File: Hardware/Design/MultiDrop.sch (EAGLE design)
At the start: 13 parts

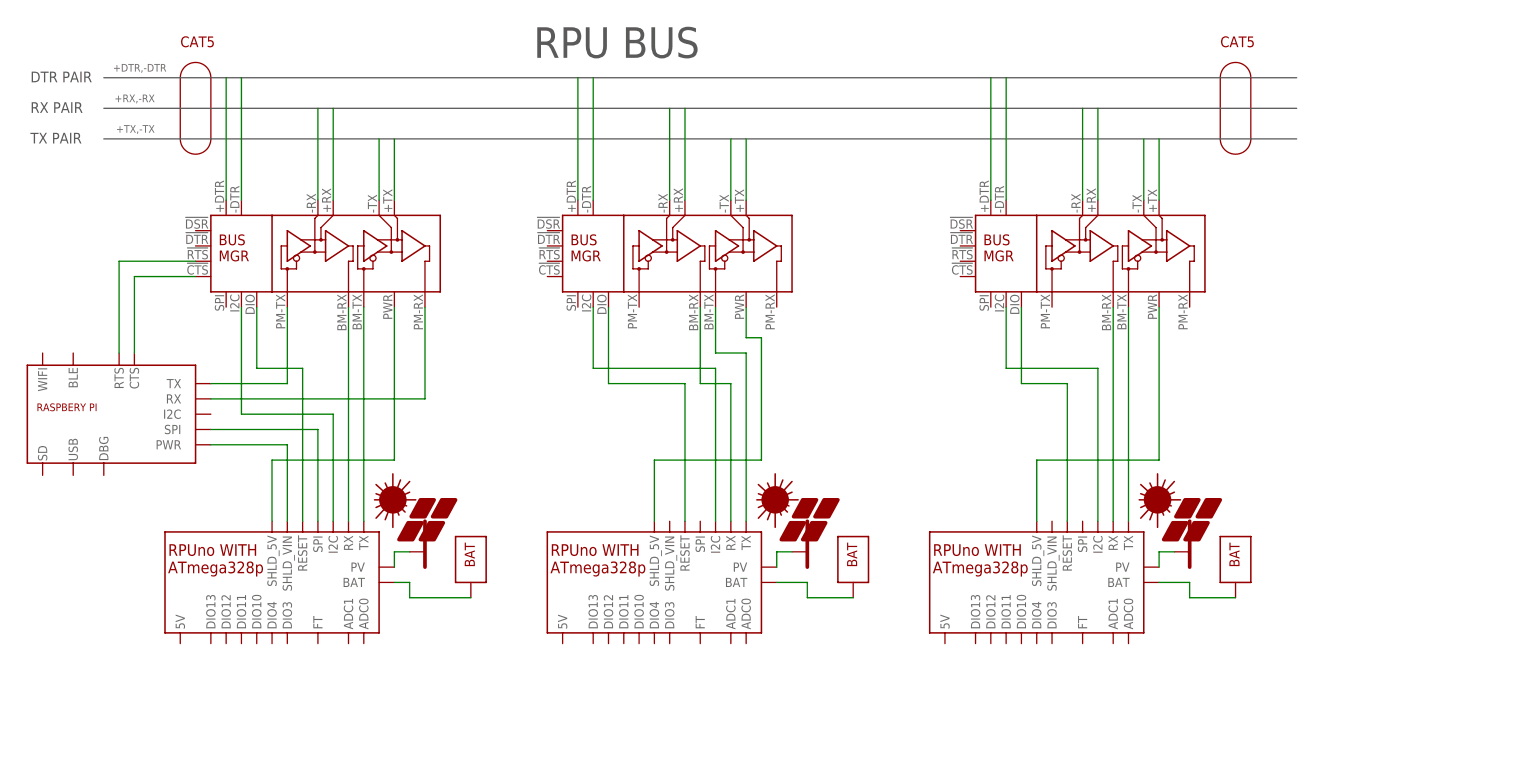
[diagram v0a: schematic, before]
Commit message: example is a little more refined
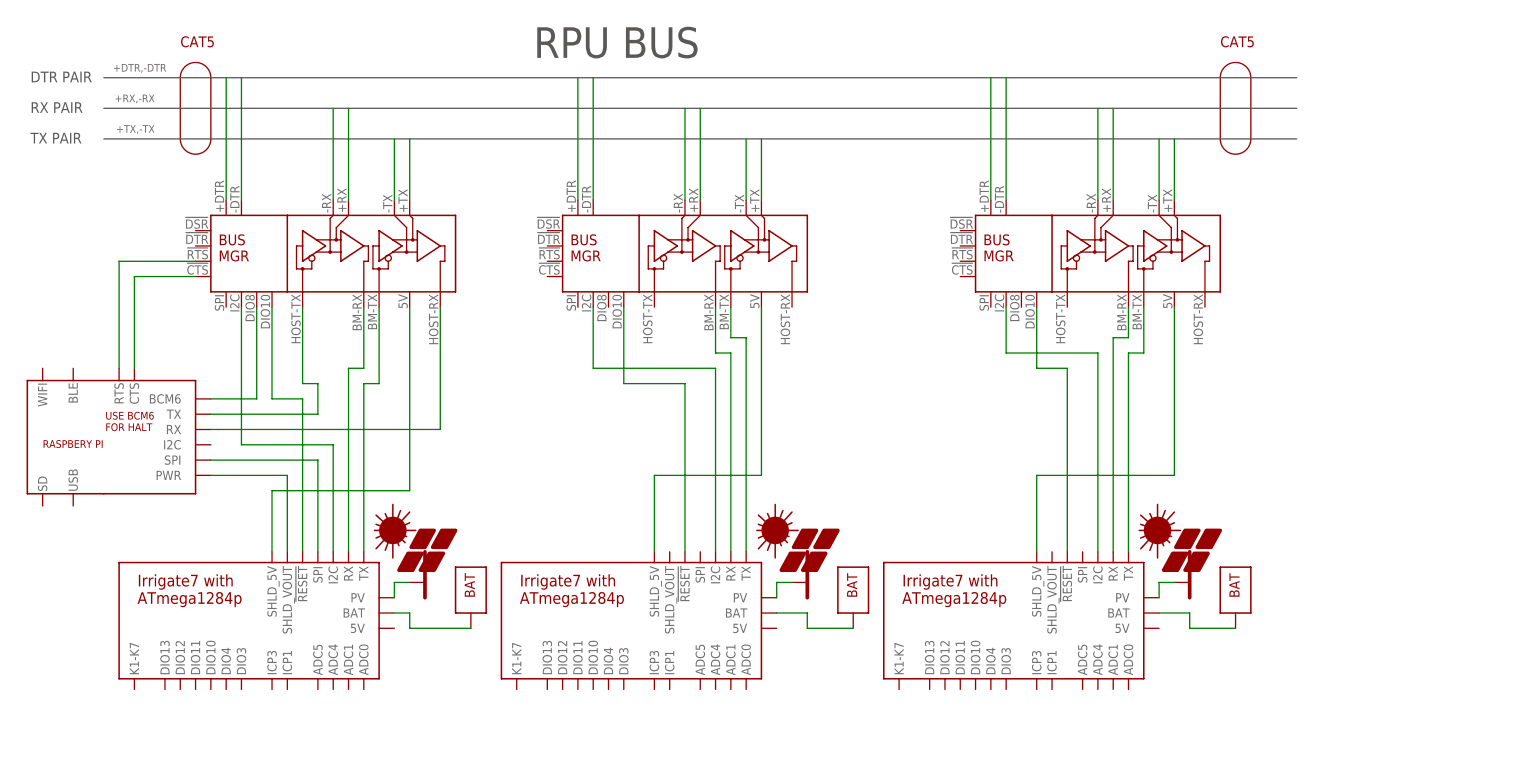
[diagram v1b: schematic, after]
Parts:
- removed BM1, BM2, BM3: (no value), Documentation:RPUNO
- added U$10: BUS_MGR, Documentation:BUS_MGR
- added U$6, U$8: IRRIGATE7, Documentation:IRRIGATE7
- U$2: value BUS_MGR -> IRRIGATE7; device Documentation:BUS_MGR -> Documentation:IRRIGATE7
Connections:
- new net N$13: U$10.DIO8, U$3.BCM6
- net +DTR: now also U$10.+DTR; no longer U$1.+DTR
- net +DTR1: now also U$5.+DTR; no longer U$2.+DTR
- net +DTR3: now also U$1.+DTR; no longer U$5.+DTR
- net +RX: now also U$10.+RX; no longer U$1.+RX
- net +RX1: now also U$5.+RX; no longer U$2.+RX
- net +RX3: now also U$1.+RX; no longer U$5.+RX
- net +TX: now also U$10.+TX; no longer U$1.+TX
- net +TX1: now also U$5.+TX; no longer U$2.+TX
- net +TX3: now also U$1.+TX; no longer U$5.+TX
- net -DTR: now also U$10.-DTR; no longer U$1.-DTR
- net -DTR1: now also U$5.-DTR; no longer U$2.-DTR
- net -DTR3: now also U$1.-DTR; no longer U$5.-DTR
- net -RX: now also U$10.-RX; no longer U$1.-RX
- net -RX1: now also U$5.-RX; no longer U$2.-RX
- net -RX3: now also U$1.-RX; no longer U$5.-RX
- net -TX: now also U$10.-TX; no longer U$1.-TX
- net -TX1: now also U$5.-TX; no longer U$2.-TX
- net -TX3: now also U$1.-TX; no longer U$5.-TX
- net N$1: now also U$10.BM_TX, U$8.TX; no longer BM2.TX, U$1.BM_TX
- net N$10: now also U$5.BM_TX, U$6.TX; no longer BM1.TX, U$2.BM_TX
- net N$11: now also U$5.BM_RX, U$6.RX; no longer BM1.RX, U$2.BM_RX
- net N$12: now also U$8.BAT; no longer BM2.BAT
- net N$14: now also U$1.BM_TX, U$2.TX; no longer BM3.TX, U$5.BM_TX
- net N$17: now also U$6.BAT; no longer BM1.BAT
- net N$2: now also U$10.BM_RX, U$8.RX; no longer BM2.RX, U$1.BM_RX
- net N$21: now also U$1.BM_RX, U$2.RX; no longer BM3.RX, U$5.BM_RX
- net N$29: now also U$10.PWR, U$8.SHLD_5V; no longer BM2.SHLD_5V, U$1.PWR
- net N$3: now also U$8.SHLD_VOUT; no longer BM2.SHLD_VIN
- net N$30: now also U$10.DIO10, U$8.!RESET; no longer BM2.RESET, U$1.DIO
- net N$31: now also U$2.BAT; no longer BM3.BAT
- net N$32: now also U$1.I2C, U$2.I2C; no longer BM3.I2C, U$5.I2C
- net N$33: now also U$10.I2C, U$8.I2C; no longer BM2.I2C, U$1.I2C
- net N$34: now also U$2.PV; no longer BM3.PV
- net N$36: now also U$6.PV; no longer BM1.PV
- net N$4: now also U$10.!CTS; no longer U$1.!CTS
- net N$41: now also U$1.PWR, U$2.SHLD_5V; no longer BM3.SHLD_5V, U$5.PWR
- net N$43: now also U$1.DIO10, U$2.!RESET; no longer BM3.RESET, U$5.DIO
- net N$44: now also U$5.DIO10, U$6.!RESET; no longer BM1.RESET, U$2.DIO
- net N$45: now also U$5.PWR, U$6.SHLD_5V; no longer BM1.SHLD_5V, U$2.PWR
- net N$48: now also U$5.I2C, U$6.I2C; no longer BM1.I2C, U$2.I2C
- net N$5: now also U$10.!RTS; no longer U$1.!RTS
- net N$6: now also U$8.SPI; no longer BM2.SPI
- net N$7: now also U$8.PV; no longer BM2.PV
- net N$8: now also U$10.HOST_RX, U$3.RX; no longer U$1.PM_RX
- net N$9: now also U$10.HOST_TX, U$3.TX; no longer U$1.PM_TX

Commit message: Hardware: ^2 dsgn in wip
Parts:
- added SW: TACTILE, S-Tactile:TAC_SW
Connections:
- new net 0V: SW.1
- new net N$15: U$10.I2C1, U$3.I2C
- net N$13: now also SW.3
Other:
- note added: "20W PV"
- note added: "3W PV"
- note added: "50 AHr"
- note added: "7.5AHr"
- note added: "PI SHUTDOWN"
- note added: "USB WiFi USB Ethernet USB OTG"

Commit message: Hardware: ^4 schmatic design
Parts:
- added BM1: (no value), Documentation:RPUNO
- added SW1, SW2: TACTILE, S-Tactile:TAC_SW
- added U$11: PI, Documentation:PI
- added U$12, U$13, U$14: POL, Documentation:POL
- U$1: value BUS_MGR -> IRRIGATE7; device Documentation:BUS_MGR -> Documentation:IRRIGATE7
- U$10, U$5: value BUS_MGR -> PI; device Documentation:BUS_MGR -> Documentation:PI
- U$2: value IRRIGATE7 -> RPULUX; device Documentation:IRRIGATE7 -> Documentation:RPULUX
- U$3: value PI -> BUS_MGR; device Documentation:PI -> Documentation:BUS_MGR
- U$6, U$8: value IRRIGATE7 -> BUS_MGR; device Documentation:IRRIGATE7 -> Documentation:BUS_MGR
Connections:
- removed net +DTR3: U$1.+DTR
- removed net +RX3: U$1.+RX
- removed net +TX3: U$1.+TX
- removed net -DTR3: U$1.-DTR
- removed net -RX3: U$1.-RX
- removed net -TX3: U$1.-TX
- new net +DTR2: U$6.+DTR
- new net +RX2: U$6.+RX
- new net +TX2: U$6.+TX
- new net -DTR2: U$6.-DTR
- new net -RX2: U$6.-RX
- new net -TX2: U$6.-TX
- new net N$16: U$11.RTS, U$8.!RTS
- new net N$18: U$2.SHLD_5V, U$3.PWR
- new net N$19: U$2.!RESET, U$3.BM-!RST!
- new net N$20: U$2.I2C, U$3.I2C0
- new net N$22: U$2.SPI, U$5.SPI
- new net N$23: U$3.SMBUS, U$5.I2C
- new net N$24: SW1.3, U$3.SHDN, U$5.BCM6
- new net N$25: U$3.!CTS, U$5.CTS
- new net N$26: U$3.!RTS, U$5.RTS
- new net N$27: BM1.TX, U$6.BM_TX
- new net N$28: BM1.RX, U$6.BM_RX
- new net N$35: BM1.!RESET, U$6.BM-!RST!
- new net N$37: BM1.SHLD_VOUT, U$14.VIN
- new net N$38: BM1.SPI, U$10.SPI
- new net N$39: U$10.I2C, U$6.SMBUS
- new net N$40: SW2.3, U$10.BCM6, U$6.SHDN
- new net N$42: U$10.RTS, U$6.!RTS
- new net N$46: BM1.0V@2, PV4.-PV, U$7.-BAT
- new net N$47: BM1.PWR, U$7.+BAT
- new net N$49: U$10.PWR, U$14.5V
- new net N$50: U$13.5V, U$5.PWR
- new net N$51: U$11.PWR, U$12.5V
- net +DTR: now also U$8.+DTR; no longer U$10.+DTR
- net +DTR1: now also U$3.+DTR; no longer U$5.+DTR
- net +RX: now also U$8.+RX; no longer U$10.+RX
- net +RX1: now also U$3.+RX; no longer U$5.+RX
- net +TX: now also U$8.+TX; no longer U$10.+TX
- net +TX1: now also U$3.+TX; no longer U$5.+TX
- net -DTR: now also U$8.-DTR; no longer U$10.-DTR
- net -DTR1: now also U$3.-DTR; no longer U$5.-DTR
- net -RX: now also U$8.-RX; no longer U$10.-RX
- net -RX1: now also U$3.-RX; no longer U$5.-RX
- net -TX: now also U$8.-TX; no longer U$10.-TX
- net -TX1: now also U$3.-TX; no longer U$5.-TX
- net 0V: now also SW1.1, SW2.1
- net N$1: now also U$1.TX, U$8.BM_TX; no longer U$10.BM_TX, U$8.TX
- net N$10: now also U$2.TX, U$3.BM_TX; no longer U$5.BM_TX, U$6.TX
- net N$11: now also U$2.RX, U$3.BM_RX; no longer U$5.BM_RX, U$6.RX
- net N$12: now also U$1.PWR, U$4.+BAT; no longer U$4.BAT_PWR, U$8.BAT
- net N$13: now also U$11.CTS, U$8.!CTS; no longer SW.3, U$10.DIO8, U$3.BCM6
- net N$14: now also U$3.HOST_RX, U$5.RX; no longer U$1.BM_TX, U$2.TX
- net N$15: now also PV1.+PV, U$1.ALT; no longer U$10.I2C1, U$3.I2C
- net N$17: now also U$3.HOST_TX, U$5.TX; no longer U$6.BAT, U$9.BAT_PWR
- net N$2: now also U$1.RX, U$8.BM_RX; no longer U$10.BM_RX, U$8.RX
- net N$21: now also U$13.VIN, U$2.SHLD_VIN; no longer U$1.BM_RX, U$2.RX
- net N$29: now also U$1.5V@SHLD, U$8.PWR; no longer U$10.PWR, U$8.SHLD_5V
- net N$3: now also U$1.VOUT, U$12.VIN; no longer U$3.PWR, U$8.SHLD_VOUT
- net N$30: now also U$1.!RESET, U$8.BM-!RST!; no longer U$10.DIO10, U$8.!RESET
- net N$31: now also U$10.RX, U$6.HOST_RX; no longer U$2.BAT, U$7.BAT_PWR
- net N$32: now also U$10.TX, U$6.HOST_TX; no longer U$1.I2C, U$2.I2C
- net N$33: now also U$1.I2C, U$8.I2C0; no longer U$10.I2C, U$8.I2C
- net N$34: now also BM1.SHLD_5V, U$6.PWR; no longer PV4.PV_PWR, U$2.PV
- net N$36: now also BM1.I2C, U$6.I2C0; no longer PV2.PV_PWR, U$6.PV
- net N$4: now also U$11.I2C, U$8.SMBUS; no longer U$10.!CTS, U$3.CTS
- net N$41: now also U$10.CTS, U$6.!CTS; no longer U$1.PWR, U$2.SHLD_5V
- net N$43: now also PV2.-PV, U$2.0V@2, U$9.-BAT; no longer U$1.DIO10, U$2.!RESET
- net N$44: now also U$2.PWR, U$9.+BAT; no longer U$5.DIO10, U$6.!RESET
- net N$45: now also PV2.+PV, U$2.ALT; no longer U$5.PWR, U$6.SHLD_5V
- net N$48: now also BM1.ALT, PV4.+PV; no longer U$5.I2C, U$6.I2C
- net N$5: now also SW.3, U$11.BCM6, U$8.SHDN; no longer U$10.!RTS, U$3.RTS
- net N$6: now also U$1.SPI, U$11.SPI; no longer U$3.SPI, U$8.SPI
- net N$7: now also PV1.-PV, U$1.0V@PWR, U$4.-BAT; no longer PV1.PV_PWR, U$8.PV
- net N$8: now also U$11.RX, U$8.HOST_RX; no longer U$10.HOST_RX, U$3.RX
- net N$9: now also U$11.TX, U$8.HOST_TX; no longer U$10.HOST_TX, U$3.TX
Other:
- note removed: "3W PV"
- note removed: "7.5AHr"
- note removed: "RPUadpt"
- note removed: "USB WiFi USB Ethernet USB OTG"
- moved on the sheet: SW
